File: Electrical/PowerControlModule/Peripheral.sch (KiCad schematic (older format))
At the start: 4 parts, among them J9 Screw_Terminal_01x02

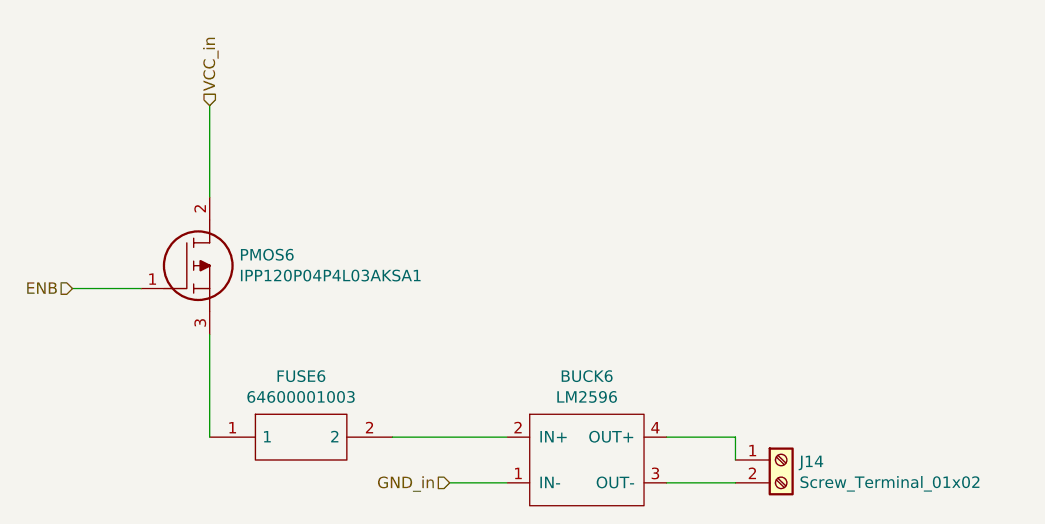
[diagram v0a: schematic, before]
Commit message: Peripheral changes and rewired PCB
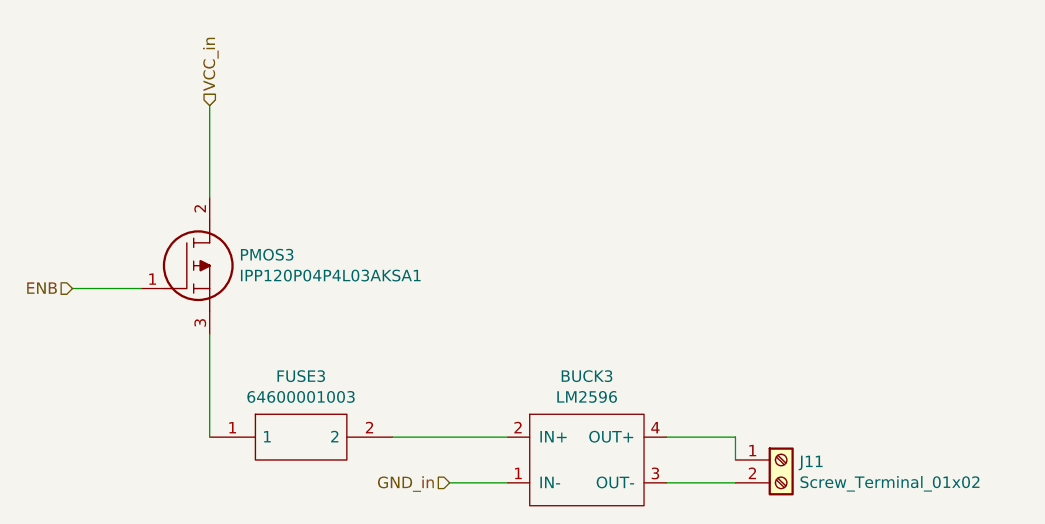
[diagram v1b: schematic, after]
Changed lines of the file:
@@
 $Descr A4 11693 8268
 encoding utf-8
-Sheet 7 11
+Sheet 4 11
 Title ""
 Date ""
@@
 AR Path="/5D99AFA5/5D952D5A" Ref="FUSE5"  Part="1"
 AR Path="/5D99AFAC/5D952D5A" Ref="FUSE6"  Part="1"
-F 0 "FUSE6" H 4400 3265 50  0000 C CNN
+F 0 "FUSE3" H 4400 3265 50  0000 C CNN
 F 1 "64600001003" H 4400 3174 50  0000 C CNN
 F 2 "LibraryLoader:646-SERIESHOLDER" H 4650 3100 50  0001 L CNN
@@
 AR Path="/5D99AFA5/5D952D73" Ref="PMOS5"  Part="1"
 AR Path="/5D99AFAC/5D952D73" Ref="PMOS6"  Part="1"
-F 0 "PMOS6" H 4130 2496 50  0000 L CNN
+F 0 "PMOS3" H 4130 2496 50  0000 L CNN
 F 1 "IPP120P04P4L03AKSA1" H 4130 2405 50  0000 L CNN
 F 2 "LibraryLoader:TO254P440X1000X2110-3P" H 4150 2300 50  0001 L CNN
@@
 AR Path="/5D992880/5D897E7B" Ref="BUCK7"  Part="1"
 AR Path="/5D992879/5D897E7B" Ref="BUCK8"  Part="1"
-F 0 "BUCK6" H 5650 2765 50  0000 C CNN
+F 0 "BUCK3" H 5650 2765 50  0000 C CNN
 F 1 "LM2596" H 5650 2674 50  0000 C CNN
 F 2 "SCR_KiCAD_Lib:LM2596" H 5650 2750 50  0001 C CNN
@@
 AR Path="/5D992880/5D8A1568" Ref="J15"  Part="1"
 AR Path="/5D992879/5D8A1568" Ref="J16"  Part="1"
-F 0 "J14" H 6580 3092 50  0000 L CNN
+F 0 "J11" H 6580 3092 50  0000 L CNN
 F 1 "Screw_Terminal_01x02" H 6580 3001 50  0000 L CNN
 F 2 "TerminalBlock_Phoenix:TerminalBlock_Phoenix_MKDS-3-2-5.08_1x02_P5.08mm_Horizontal" H 6500 3100 50  0001 C CNN
